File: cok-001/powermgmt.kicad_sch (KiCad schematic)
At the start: 51 parts, among them J6004 +12V_MAIN, J6005 +5V_EVER, Q6001 FDQ7238AS, Q6002 FDQ7238AS, Q6003 DTC144E, Q6004 SI3493, Q6009 UMH2NTN, Q6010 SI4943, U6003 MB39A, U6008 NCP511SN18T1, U6011 NCP511, U6012 MM3141, U6013 MM1562, U6014 MM1591, U6019 NCP511SN18T1, U6021 MM1591, U6022 MM1593

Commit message: pcb update
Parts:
- added C6009: 50V, Capacitor_SMD:C_0402_1005Metric, symbol Device:C
- added C6011: 680p, Capacitor_SMD:C_0402_1005Metric, symbol Device:C
- added C6036, C6037: 16V, Capacitor_SMD:C_0402_1005Metric, symbol Device:C
- added C6039: 1u 16V, Capacitor_SMD:C_0603_1608Metric, symbol Device:C
- added R6022: 47k, Resistor_SMD:R_0603_1608Metric, symbol Device:R_US
- added R6033: 1500, Resistor_SMD:R_0402_1005Metric, symbol Device:R_US
- added R6034: 2400, Resistor_SMD:R_0402_1005Metric, symbol Device:R_US
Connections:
- net GND: now also C6039.2
- net at U6003.1 (-INE1): now also C6009.1, R6022.2
- net at U6003.2 (FB1): now also C6011.2
- net at U6003.23 (ILIM2): now also C6037.2, R6034.1
- net at U6003.24 (VCC): now also C6036.2, C6037.1, C6039.1, R6033.2, R6034.2
- net at U6003.25 (ILIM1): now also C6036.1, R6033.1
- new net: C6009.2, C6011.1, R6022.1

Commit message: regulator
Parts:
- added C6002: 1u 16V, Capacitor_SMD:C_0603_1608Metric, symbol Device:C
- added C6004: XX, Capacitor_SMD:C_0402_1005Metric, symbol Device:C
- added C6022: 0.001u 50V, Capacitor_SMD:C_0402_1005Metric, symbol Device:C
- added C6032: 0.022u 16V, Capacitor_SMD:C_0402_1005Metric, symbol Device:C
- added Q6006: UMH2NTN, Package_TO_SOT_SMD:SOT-363_SC-70-6, symbol Transistor_BJT:UMH3N
- added Q6007, Q6008: SI3493, Package_SO:TSOP-6_1.65x3.05mm_P0.95mm, symbol Transistor_FET:PMN48XP
- added Q6012: Si3460DV, Package_SO:TSOP-6_1.65x3.05mm_P0.95mm, symbol Transistor_FET:Si3456DDV
- added R6001: 3600, Resistor_SMD:R_0402_1005Metric, symbol Device:R_US
- added R6002: 2700, Resistor_SMD:R_0402_1005Metric, symbol Device:R_US
- added R6018: 200k, Resistor_SMD:R_0402_1005Metric, symbol Device:R_US
- added R6019: 0, Resistor_SMD:R_0402_1005Metric, symbol Device:R_US
- added R6020: 360k, Resistor_SMD:R_0402_1005Metric, symbol Device:R_US
- added R6032: 10k, Resistor_SMD:R_0603_1608Metric, symbol Device:R_US
- added R6060, R6061: 100k, Resistor_SMD:R_0603_1608Metric, symbol Device:R_US
- added R6063, R6064: 150k, Resistor_SMD:R_0603_1608Metric, symbol Device:R_US
- added R6524, R6525: 1k, Resistor_SMD:R_0603_1608Metric, symbol Device:R_US
- added U6004, U6023: PST3642UL, Package_TO_SOT_SMD:SC-82AB, symbol PS3:PST36XX
- added U6005, U6009: NCP511SN33T1G, Package_TO_SOT_SMD:SOT-23-5, symbol Regulator_Linear:MIC5219-3.3YM5
- added U6006: NCP511SN18T1, Package_TO_SOT_SMD:SOT-23-5, symbol Regulator_Linear:MIC5219-3.3YM5
- added U6007: TPS73101DBV, Package_TO_SOT_SMD:SOT-23-5, symbol Regulator_Linear:TPS73101DBV
- added U6017: BD3521, Package_SO:MSOP-8_3x3mm_P0.65mm, symbol PS3:BD35xxFVM-TR
- R6022, R6029, R6030: footprint Resistor_SMD:R_0603_1608Metric -> Resistor_SMD:R_0402_1005Metric
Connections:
- net +12V_MAIN: now also R6001.2
- net +3.3V_MISC: now also U6007.1 (IN)
- net +5V_EVER: now also C6022.1, U6004.2 (VDD), U6005.1 (IN), U6006.1 (IN), U6009.1 (IN)
- net GND: now also C6022.2, C6032.2, Q6006.1 (E1), Q6006.4 (E2), R6524.1, R6525.1, U6004.1 (GND), U6005.2 (GND), U6006.2 (GND), U6007.2 (GND), U6009.2 (GND)
- net SW_4_B: now also Q6006.5 (B2)
- net SW_8_B: now also U6007.3 (EN)
- net SW_ATA: now also Q6006.2 (B1)
- new net: Q6012.1 (D), Q6012.2 (D), Q6012.5 (D), Q6012.6 (D)
- new net: Q6012.3 (G), U6017.7 (G)
- new net: C6002.2, C6004.2, R6002.1, R6020.1, U6023.1 (GND)
- new net: R6019.1, R6020.2
- new net: C6002.1, R6001.1, R6002.2, R6018.2, U6023.2 (VDD)
- new net: C6032.1, U6004.3 (Cd)
- new net: Q6006.3 (C2), R6061.1, R6064.1
- new net: Q6007.3 (G), R6063.2
- new net: Q6007.4 (S), R6060.2
- new net: Q6008.3 (G), R6064.2
- new net: Q6008.4 (S), R6061.2
- new net: C6004.1, U6023.3 (Cd)
- new net: Q6006.6 (C1), R6060.1, R6063.1
- new net +1.6V_BE_VDDA: U6007.5 (OUT)
- new net +3.3V_EVER: R6032.2
- new net +5V_HDD: Q6007.1 (D), Q6007.2 (D), Q6007.5 (D), Q6007.6 (D), R6524.2
- new net +5V_USB: Q6008.1 (D), Q6008.2 (D), Q6008.5 (D), Q6008.6 (D), R6525.2
- new net ~{POW_FAIL}: R6018.1, R6019.2, U6023.4 (OUT)
- new net ~{SYSCON_RST}: R6032.1, U6004.4 (OUT), U6009.3 (EN)
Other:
- moved on the sheet: C6009, C6010, C6011, C6021, C6023, C6024, C6025, C6027, C6029, C6036, C6037, C6039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

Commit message: msop
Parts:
- U6017: footprint Package_SO:MSOP-8_3x3mm_P0.65mm -> PS3:MSOP-8_2.9x4mm_P0.65mm
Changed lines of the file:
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@@
 			)
 		)
-		(property "Footprint" "Package_SO:MSOP-8_3x3mm_P0.65mm"
+		(property "Footprint" "PS3:MSOP-8_2.9x4mm_P0.65mm"
 			(at 332.74 139.7 0)
 			(effects

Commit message: button connector
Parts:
- added TP9623: TestPoint, TestPoint:TestPoint_Pad_D1.5mm, symbol Connector:TestPoint
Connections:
- net ACDC_STBY: now also TP9623.1
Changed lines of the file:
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@@
 	)
 	(junction
+		(at 27.94 33.02)
+		(diameter 0)
+		(color 0 0 0 0)
+	)
+	(junction
 		(at 82.55 171.45)
 		(diameter 0)
@@
 	(wire
 		(pts
-			(xy 22.86 33.02) (xy 34.29 33.02)
+			(xy 22.86 33.02) (xy 27.94 33.02)
 		)
 		(stroke
@@
 	(wire
 		(pts
+			(xy 27.94 33.02) (xy 34.29 33.02)
+		)
+		(stroke
+			(width 0)
+			(type default)
+		)
+	)
+	(wire
+		(pts
 			(xy 237.49 254) (xy 242.57 254)
 		)
@@
 					(unit 1)
 				)
+			)
+		)
+	)
+	(symbol
+		(lib_id "Connector:TestPoint")
+		(at 27.94 33.02 180)
+		(unit 1)
+		(exclude_from_sim no)
+		(in_bom yes)
+		(on_board yes)
+		(dnp no)
+		(property "Reference" "TP9623"
+			(at 27.94 41.402 90)
+			(effects
+				(font
+					(size 1.27 1.27)
+				)
+			)
+		)
+		(property "Value" "TestPoint"
+			(at 25.4 36.322 90)
+			(effects
+				(font
+					(size 1.27 1.27)
+				)
+				(hide yes)
+			)
+		)
+		(property "Footprint" "TestPoint:TestPoint_Pad_D1.5mm"
+			(at 22.86 33.02 0)
+			(effects
+				(font
+					(size 1.27 1.27)
+				)
+				(hide yes)
+			)
+		)
+		(property "Datasheet" "~"
+			(at 22.86 33.02 0)
+			(effects
+				(font
+					(size 1.27 1.27)
+				)
+				(hide yes)
+			)
+		)
+		(property "Description" "test point"
+			(at 27.94 33.02 0)
+			(effects
+				(font
+					(size 1.27 1.27)
+				)
+				(hide yes)
+			)
+		)
+		(pin "1"
+		)
+		(instances
+			(project "cok-001"
+				(path "/976eb78d-8215-4cc0-9d72-f9d535c7970b/be970d6c-aeec-4303-8a86-89c9df8950fa"
+					(reference "TP9623")
+					(unit 1)
+				)

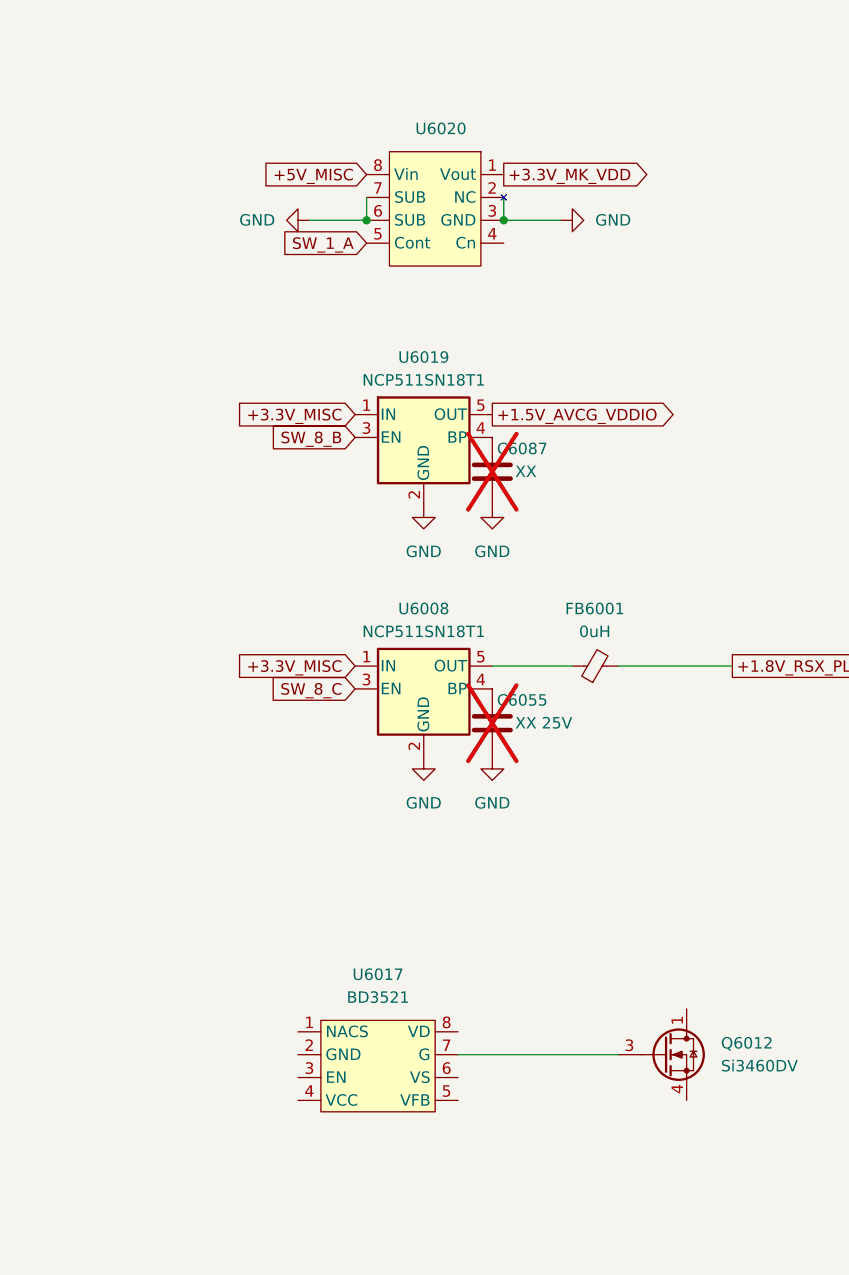
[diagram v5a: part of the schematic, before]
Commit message: power flags
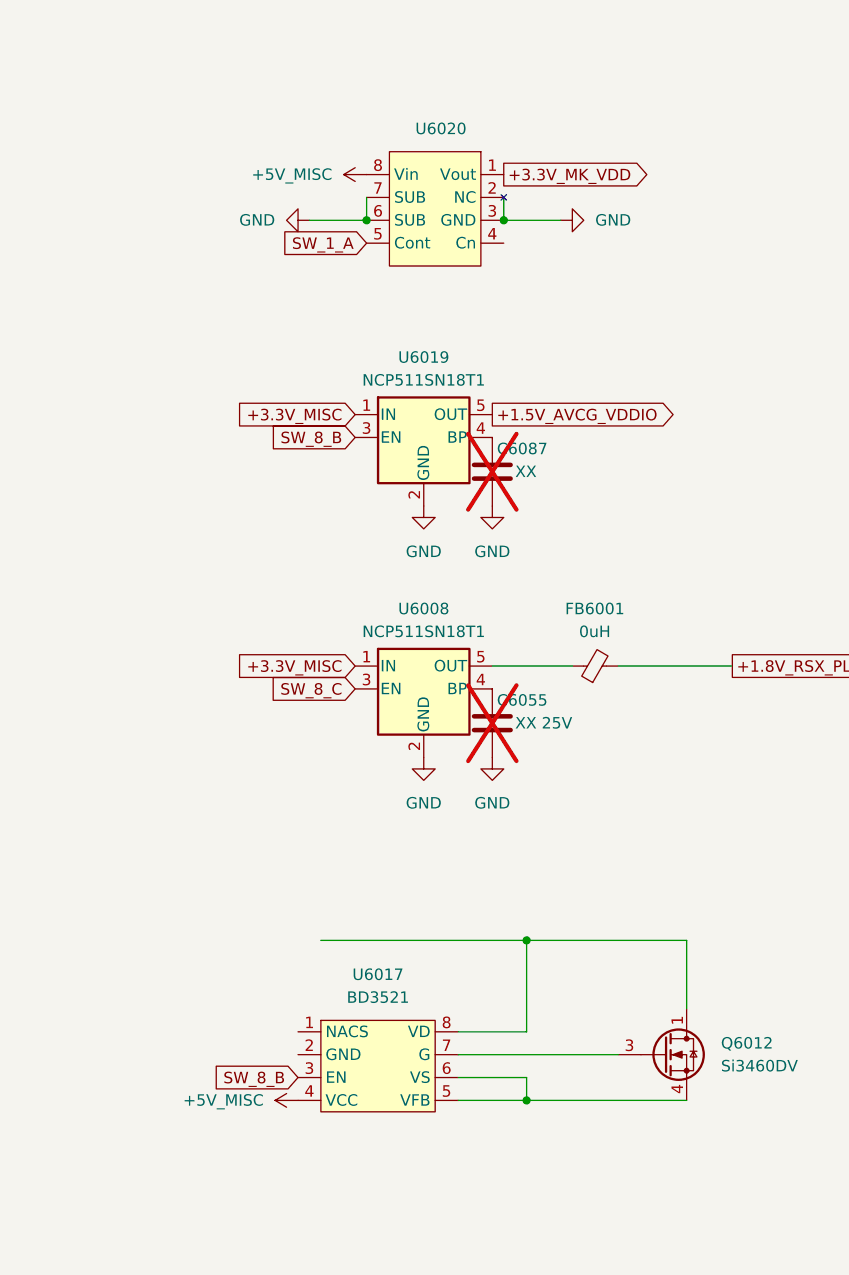
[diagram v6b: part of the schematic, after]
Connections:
- net +5V_MISC: now also U6017.4 (VCC)
- net SW_8_B: now also U6017.3 (EN)
- net at Q6012.1 (D), Q6012.2 (D), Q6012.5 (D)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: now also U6017.8 (VD)
- net at Q6012.4 (S): now also U6017.5 (VFB), U6017.6 (VS)
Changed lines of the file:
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@@
 	)
 	(junction
+		(at 358.14 147.32)
+		(diameter 0)
+		(color 0 0 0 0)
+	)
+	(junction
 		(at 22.86 29.21)
 		(diameter 0)
@@
 	)
 	(junction
+		(at 358.14 129.54)
+		(diameter 0)
+		(color 0 0 0 0)
+	)
+	(junction
 		(at 227.33 246.38)
 		(diameter 0)
@@
 	(wire
 		(pts
+			(xy 350.52 147.32) (xy 358.14 147.32)
+		)
+		(stroke
+			(width 0)
+			(type default)
+		)
+	)
+	(wire
+		(pts
 			(xy 74.93 250.19) (xy 74.93 269.24)
 		)
@@
 	(wire
 		(pts
+			(xy 375.92 137.16) (xy 375.92 129.54)
+		)
+		(stroke
+			(width 0)
+			(type default)
+		)
+	)
+	(wire
+		(pts
 			(xy 50.8 66.04) (xy 60.96 66.04)
 		)
@@
 	(wire
 		(pts
+			(xy 335.28 129.54) (xy 358.14 129.54)
+		)
+		(stroke
+			(width 0)
+			(type default)
+		)
+	)
+	(wire
+		(pts
 			(xy 91.44 73.66) (xy 101.6 73.66)
 		)
@@
 	(wire
 		(pts
+			(xy 358.14 129.54) (xy 375.92 129.54)
+		)
+		(stroke
+			(width 0)
+			(type default)
+		)
+	)
+	(wire
+		(pts
 			(xy 128.27 229.87) (xy 128.27 233.68)
 		)
@@
 	(wire
 		(pts
+			(xy 358.14 147.32) (xy 375.92 147.32)
+		)
+		(stroke
+			(width 0)
+			(type default)
+		)
+	)
+	(wire
+		(pts
 			(xy 107.95 207.01) (xy 107.95 171.45)
 		)
@@
 	(wire
 		(pts
+			(xy 358.14 139.7) (xy 358.14 129.54)
+		)
+		(stroke
+			(width 0)
+			(type default)
+		)
+	)
+	(wire
+		(pts
 			(xy 218.44 213.36) (xy 224.79 213.36)
 		)
@@
 	(wire
 		(pts
+			(xy 350.52 139.7) (xy 358.14 139.7)
+		)
+		(stroke
+			(width 0)
+			(type default)
+		)
+	)
+	(wire
+		(pts
 			(xy 207.01 269.24) (xy 227.33 269.24)
 		)
@@
 	(wire
 		(pts
+			(xy 358.14 144.78) (xy 358.14 147.32)
+		)
+		(stroke
+			(width 0)
+			(type default)
+		)
+	)
+	(wire
+		(pts
+			(xy 350.52 144.78) (xy 358.14 144.78)
+		)
+		(stroke
+			(width 0)
+			(type default)
+		)
+	)
+	(wire
+		(pts
 			(xy 246.38 213.36) (xy 240.03 213.36)
 		)
@@
 		)
 	)
+	(global_label "SW_8_B"
+		(shape input)
+		(at 332.74 144.78 180)
+		(fields_autoplaced yes)
+		(effects
+			(font
+				(size 1.27 1.27)
+			)
+			(justify right)
+		)
+		(property "Intersheetrefs" "${INTERSHEET_REFS}"
+			(at 322.6792 144.78 0)
+			(effects
+				(font
+					(size 1.27 1.27)
+				)
+				(justify right)
+				(hide yes)
+			)
+		)
+	)
 	(global_label "+3.3V_MK_VDD"
 		(shape output)
@@
 		)
 	)
-	(global_label "+5V_MISC"
-		(shape input)
-		(at 340.36 44.45 180)
-		(fields_autoplaced yes)
-		(effects
-			(font
-				(size 1.27 1.27)
-			)
-			(justify right)
-		)
-		(property "Intersheetrefs" "${INTERSHEET_REFS}"
-			(at 328.001 44.45 0)
-			(effects
-				(font
-					(size 1.27 1.27)
-				)
-				(justify right)
-				(hide yes)
-			)
-		)
-	)
 	(symbol
 		(lib_id "power:GND")
@@
 					(unit 1)
 				)
+			)
+		)
+	)
+	(symbol
+		(lib_id "power:+5V")
+		(at 340.36 44.45 90)
+		(unit 1)
+		(exclude_from_sim no)
+		(in_bom yes)
+		(on_board yes)
+		(dnp no)
+		(fields_autoplaced yes)
+		(property "Reference" "#PWR06001"
+			(at 344.17 44.45 0)
+			(effects
+				(font
+					(size 1.27 1.27)
+				)
+				(hide yes)
+			)
+		)
+		(property "Value" "+5V_MISC"
+			(at 336.55 44.4499 90)
+			(effects
+				(font
+					(size 1.27 1.27)
+				)
+				(justify left)
+			)
+		)
+		(property "Footprint" ""
+			(at 340.36 44.45 0)
+			(effects
+				(font
+					(size 1.27 1.27)
+				)
+				(hide yes)
+			)
+		)
+		(property "Datasheet" ""
+			(at 340.36 44.45 0)
+			(effects
+				(font
+					(size 1.27 1.27)
+				)
+				(hide yes)
+			)
+		)
+		(property "Description" "Power symbol creates a global label with name \"+5V\""
+			(at 340.36 44.45 0)
+			(effects
+				(font
+					(size 1.27 1.27)
+				)
+				(hide yes)
+			)
+		)
+		(pin "1"
+		)
+		(instances
+			(project "cok-001"
+				(path "/976eb78d-8215-4cc0-9d72-f9d535c7970b/be970d6c-aeec-4303-8a86-89c9df8950fa"
+					(reference "#PWR06001")
+					(unit 1)
+				)
+			)
+		)
+	)
+	(symbol
+		(lib_id "power:+5V")
+		(at 332.74 147.32 90)
+		(unit 1)
+		(exclude_from_sim no)
+		(in_bom yes)
+		(on_board yes)
+		(dnp no)
+		(fields_autoplaced yes)
+		(property "Reference" "#PWR06002"
+			(at 336.55 147.32 0)
+			(effects
+				(font
+					(size 1.27 1.27)
+				)
+				(hide yes)
+			)
+		)
+		(property "Value" "+5V_MISC"
+			(at 328.93 147.3199 90)
+			(effects
+				(font
+					(size 1.27 1.27)
+				)
+				(justify left)
+			)
+		)
+		(property "Footprint" ""
+			(at 332.74 147.32 0)
+			(effects
+				(font
+					(size 1.27 1.27)
+				)
+				(hide yes)
+			)
+		)
+		(property "Datasheet" ""
+			(at 332.74 147.32 0)
+			(effects
+				(font
+					(size 1.27 1.27)
+				)
+				(hide yes)
+			)
+		)
+		(property "Description" "Power symbol creates a global label with name \"+5V\""
+			(at 332.74 147.32 0)
+			(effects
+				(font
+					(size 1.27 1.27)
+				)
+				(hide yes)
+			)
+		)
+		(pin "1"
+		)
+		(instances
+			(project "cok-001"
+				(path "/976eb78d-8215-4cc0-9d72-f9d535c7970b/be970d6c-aeec-4303-8a86-89c9df8950fa"
+					(reference "#PWR06002")
+					(unit 1)
+				)

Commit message: caps
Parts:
- added C6050, C6056, C6075, C6080, C6082, C6091: 2.2u 10V, Capacitor_SMD:C_0805_2012Metric, symbol Device:C
- added C6057, C6078: 1u 10V, Capacitor_SMD:C_0402_1005Metric, symbol Device:C
- added C6061, C6062, C6063, C6073, C6076: 0.1u 10V, Capacitor_SMD:C_0402_1005Metric, symbol Device:C
- added C6079: XX 16V, Capacitor_SMD:C_0402_1005Metric, symbol Device:C
- added C6084, C6093: 0.022u 16V, Capacitor_SMD:C_0402_1005Metric, symbol Device:C
- added C6085: XX 25V, Capacitor_SMD:C_0402_1005Metric, symbol Device:C
- added C6088: 470p, Capacitor_SMD:C_0402_1005Metric, symbol Device:C
- added C6089: 10u 6.3V, Capacitor_SMD:C_0805_2012Metric, symbol Device:C
- added C6090, C6096, C6500: 100p, Capacitor_SMD:C_0402_1005Metric, symbol Device:C
- added C6095: 220u 2.5V, Capacitor_Tantalum_SMD:CP_EIA-3528-21_Kemet-B, symbol Device:C_Polarized_US
- added R6039, R6043: XX, Resistor_SMD:R_0402_1005Metric, symbol Device:R_US
- added R6079, R6083: 100k, Resistor_SMD:R_0402_1005Metric, symbol Device:R_US
- added R6081, R6085: 150k, Resistor_SMD:R_0402_1005Metric, symbol Device:R_US
- added R6084: 220, Resistor_SMD:R_0402_1005Metric, symbol Device:R_US
- added R6098: 390, Resistor_SMD:R_0402_1005Metric, symbol Device:R_US
- added R6100: 82, Resistor_SMD:R_0402_1005Metric, symbol Device:R_US
- added TP6048, TP6053, TP6056, TP9656: TestPoint, TestPoint:TestPoint_Pad_1.0x1.0mm, symbol Connector:TestPoint
- TH6001, TH6002: symbol Device:Fuse -> Device:Thermistor
- U6020: value ~ -> MM1593DFBEG
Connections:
- net +1.5V_AVCG_VDDIO: now also C6091.1, R6100.2, TP6056.1
- net +1.8V_RSX_PLL_VDD: now also C6057.1, C6061.1, C6062.1, C6063.1, C6073.1
- net +12V_BD: now also R6039.2
- net +3.3V_MISC: now also C6050.1, C6082.1
- net +3.3V_MK_VDD: now also C6089.1, R6098.2, TP6053.1
- net +5V_BD: now also R6043.2
- net +5V_MISC: now also C6078.1, C6080.1
- net GND: now also U6017.2 (GND), C6050.2, C6056.2, C6057.2, C6061.2, C6062.2, C6063.2, C6073.2, C6075.2, C6076.1, C6078.2, C6079.2, C6080.2, C6082.2, C6084.2, C6085.2, C6088.2, C6089.2, C6090.2, C6091.2, C6093.2, C6095.2, C6096.2, C6500.2, R6039.1, R6043.1, R6098.1, R6100.1
- net SW_1_A: now also C6090.1
- net SW_8_B: now also C6096.1
- net SW_ATA: now also C6500.1
- net +1.7V_MISC: now reaches Q6012.1 (D), Q6012.2 (D), Q6012.5 (D), Q6012.6 (D), U6017.8 (VD)
- net +1.7V_MISC: now also C6075.1
- net at Q6012.3 (G), U6017.7 (G): now also R6084.2
- net +1.5V_RSX_VDDIO: now reaches Q6012.4 (S), U6017.5 (VFB), U6017.6 (VS)
- net +1.5V_RSX_VDDIO: now also C6093.1, C6095.1, TP9656.1
- net at Q6010.3 (S2), TH6001.2: now also R6083.2
- net at Q6010.4 (G2): now also C6085.1, R6085.2
- net at Q6010.1 (S1), TH6002.2: now also R6079.2
- net at Q6010.2 (G1): now also C6079.1, R6081.2
- net at U6020.4 (Cn): now also C6088.1
- net at FB6001.1, U6008.5 (OUT): now also C6056.1, TP6048.1
- net at U6017.1 (NACS): now also C6076.2
- net at Q6009.6 (C1): now also R6079.1, R6081.1
- net at Q6009.3 (C2): now also R6083.1, R6085.1
- new net: C6084.1, R6084.1
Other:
- moved on the sheet: C6055, C6087, FB6001, Q6009A, Q6009B, TH6001, TH6002, U6008, U6019, U6020

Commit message: voltage symbols
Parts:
- TP6056: footprint TestPoint:TestPoint_Pad_1.0x1.0mm -> TestPoint:TestPoint_Pad_D1.0mm
